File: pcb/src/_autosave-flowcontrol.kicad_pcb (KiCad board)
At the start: 2 copper layers, 89 x 59 mm, 42 parts, among them J1 Fan 3, J10 Fan 1, J11 Fan 2, J2 Fan 4, J3 Temp Sensor (10k Thermistor), J4 Temp Sensor (10k Thermistor), J5 Internal USB, J6 Molex 4 Pin, J7 4 Pin DRGB LED, J8 Fan 5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

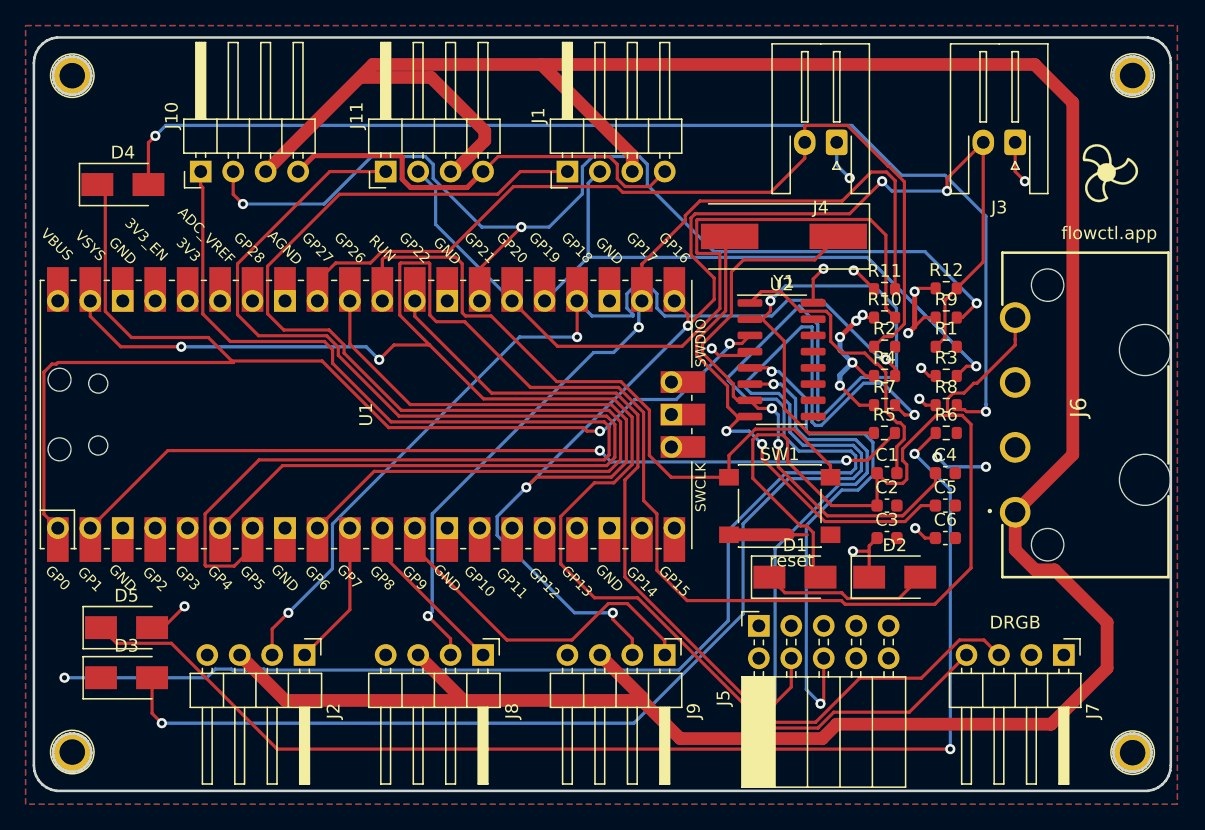
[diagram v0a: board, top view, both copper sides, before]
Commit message: add silkscreen for components
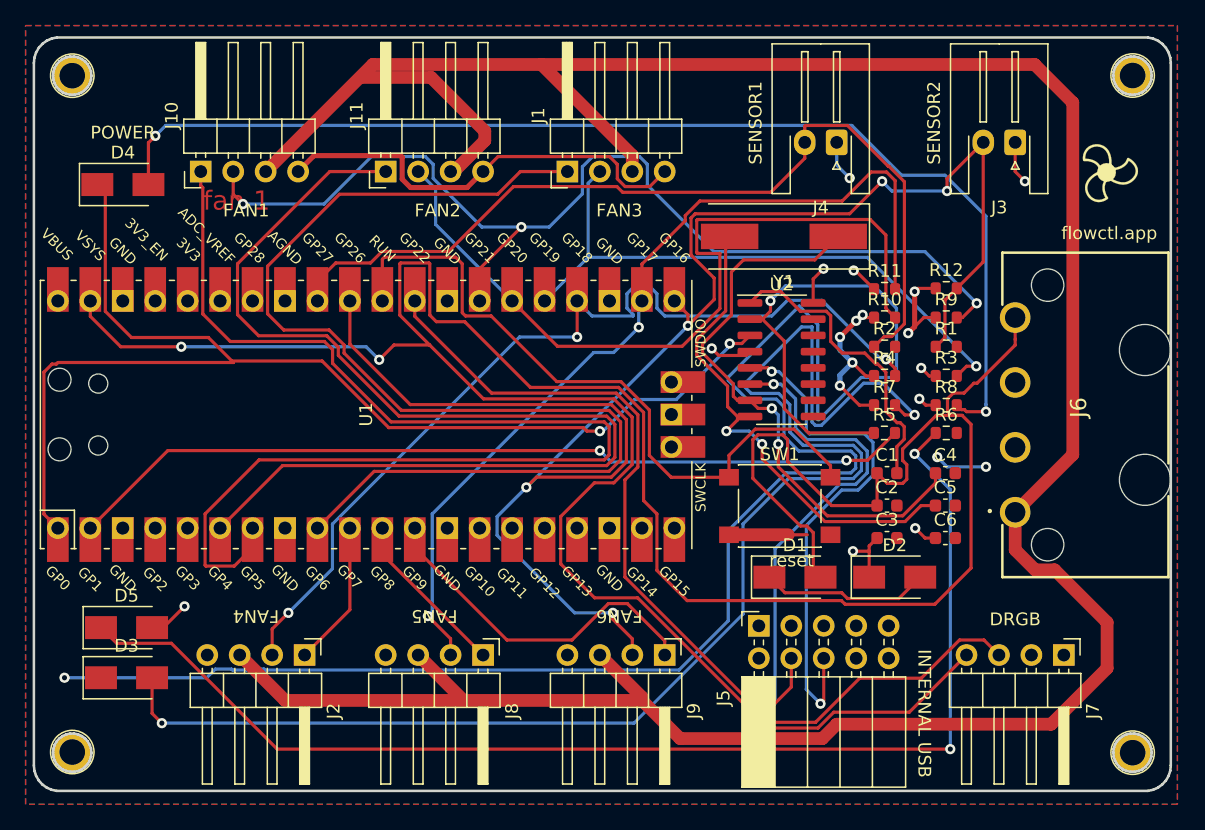
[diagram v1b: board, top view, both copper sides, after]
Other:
- board text added: "FAN1"
- board text added: "FAN2"
- board text added: "FAN3"
- board text added: "FAN4"
- board text added: "FAN5"
- board text added: "FAN6"
- board text added: "INTERNAL USB"
- board text added: "POWER"
- board text added: "SENSOR1"
- board text added: "SENSOR2"
- board text added: "fan 1"
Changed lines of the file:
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@@
   (general
     (thickness 1.6)
-    (drawings 167)
+    (drawings 178)
     (tracks 670)
     (zones 0)
@@
   (page A4)
   (layers
-    (0 F.Cu signal)
-    (31 B.Cu signal)
+    (0 F.Cu signal hide)
+    (31 B.Cu signal hide)
     (32 B.Adhes user)
     (33 F.Adhes user)
@@
     )
   )
+  (gr_text POWER (at 105.41 71.882) (layer F.SilkS)
+    (effects (font (size 1 1) (thickness 0.25)))
+  )
+  (gr_text SENSOR2 (at 168.91 71.12 90) (layer F.SilkS)
+    (effects (font (size 1 1) (thickness 0.25)))
+  )
+  (gr_text SENSOR1 (at 154.94 71.12 90) (layer F.SilkS)
+    (effects (font (size 1 1) (thickness 0.25)))
+  )
+  (gr_text DRGB (at 175.26 109.982) (layer F.SilkS)
+    (effects (font (size 1 1) (thickness 0.25)))
+  )
+  (gr_text "INTERNAL USB" (at 168.148 117.348 -90) (layer F.SilkS)
+    (effects (font (size 1 1) (thickness 0.25)))
+  )
+  (gr_text FAN6 (at 144.272 109.728 180) (layer F.SilkS)
+    (effects (font (size 1 1) (thickness 0.25)))
+  )
+  (gr_text FAN5 (at 129.794 109.728 180) (layer F.SilkS)
+    (effects (font (size 1 1) (thickness 0.25)))
+  )
+  (gr_text FAN4 (at 115.824 109.728 180) (layer F.SilkS)
+    (effects (font (size 1 1) (thickness 0.25)))
+  )
+  (gr_text FAN3 (at 144.272 77.978) (layer F.SilkS)
+    (effects (font (size 1 1) (thickness 0.25)))
+  )
+  (gr_text FAN2 (at 130.048 77.978) (layer F.SilkS)
+    (effects (font (size 1 1) (thickness 0.25)))
+  )
+  (gr_text FAN1 (at 115.062 77.978) (layer F.SilkS)
+    (effects (font (size 1 1) (thickness 0.25)))
+  )
+  (gr_text "fan 1" (at 114.3 77.216) (layer F.Cu)
+    (effects (font (size 1.5 1.5) (thickness 0.3)))
+  )
   (gr_text flowctl.app (at 182.626 79.756) (layer F.SilkS)
     (effects (font (size 1 1) (thickness 0.15)))
@@
     (effects (font (size 1 1) (thickness 0.15)) (justify mirror))
   )
-  (gr_text DRGB (at 175.26 110.236) (layer F.SilkS)
-    (effects (font (size 1 1) (thickness 0.15)))
-  )
   (gr_text "revision 4\n" (at 110.849535 69.461311) (layer B.SilkS)
     (effects (font (size 0.75 0.75) (thickness 0.1)) (justify mirror))
@@
     (connect_pads (clearance 0.089))
     (min_thickness 0.089)
-    (fill yes (arc_segments 32) (thermal_gap 0.508) (thermal_bridge_width 0.508))
+    (fill (arc_segments 32) (thermal_gap 0.508) (thermal_bridge_width 0.508))
     (polygon
       (pts
@@
     (connect_pads (clearance 0.089))
     (min_thickness 0.089)
-    (fill yes (arc_segments 32) (thermal_gap 0.508) (thermal_bridge_width 0.508))
+    (fill (arc_segments 32) (thermal_gap 0.508) (thermal_bridge_width 0.508))
     (polygon
       (pts
